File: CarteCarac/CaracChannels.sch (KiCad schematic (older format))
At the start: 6 parts

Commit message: Routé, verif pre-envoie
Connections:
- net +34 is gone; now on net +R34: SW_X32-34.3
- net -32 is gone; now on net +R34: SW_X32-34.12
- net -34 is gone; now on net -R34: SW_X32-34.11, SW_X32-34.6
- net -R32 is gone; now on net +R34: SW_X32-34.4
- net In2N is gone; now on net +R34: SW_X32-34.15, SW_X32-34.16
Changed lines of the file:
@@
 $Descr A4 11693 8268
 encoding utf-8
-Sheet 5 5
+Sheet 3 5
 Title "SCM Channels"
 Date "2019-10-22"
@@
 Comment4 "Route de Saclay \\nF-91128 Palaiseau \\nFrance"
 $EndDescr
-Text HLabel 3450 2450 2    50   Input ~ 0
+Text HLabel 3525 2450 2    50   Input ~ 0
 Pot_Offset2
-Text HLabel 3450 2050 2    50   Input ~ 0
+Text HLabel 3525 2050 2    50   Input ~ 0
 Pot_Offset1
 Connection ~ 2075 2050
@@
 	3250 2850 3375 2850
 Wire Wire Line
-	3450 2050 3250 2050
-Wire Wire Line
-	3450 2450 3250 2450
+	3525 2050 3250 2050
+Wire Wire Line
+	3525 2450 3250 2450
 Text Label 3375 2950 0    50   ~ 0
 +32
 Text Label 3375 3350 0    50   ~ 0
 -32
-Text Label 3300 2550 0    50   ~ 0
+Text Label 3375 2550 0    50   ~ 0
 -34
-Text Label 3300 2150 0    50   ~ 0
+Text Label 3400 2150 0    50   ~ 0
 +34
 Wire Wire Line
-	3250 2550 3300 2550
-Wire Wire Line
-	3250 2150 3300 2150
+	3250 2550 3375 2550
+Wire Wire Line
+	3250 2150 3400 2150
 Wire Wire Line
 	3250 3350 3375 3350
@@
 	3250 2950 3375 2950
 Wire Wire Line
-	3250 3150 3650 3150
-Wire Wire Line
-	3250 2750 3650 2750
-Wire Wire Line
-	3650 2350 3250 2350
-Wire Wire Line
-	3650 1950 3250 1950
+	3250 3150 4100 3150
+Wire Wire Line
+	3250 2750 4050 2750
+Wire Wire Line
+	4100 2350 4050 2350
+Wire Wire Line
+	4100 1950 3250 1950
 Wire Wire Line
 	2250 3250 2350 3250
@@
 AR Path="/5D6520CE/5D843251/5E294A95" Ref="RV_Z32-34"  Part="1"
 AR Path="/5D6520CE/5D83A418/5E294A95" Ref="RV_Y32-34"  Part="1"
-F 0 "RV_X32-34" V 1868 2250 50  0000 C CNN
+F 0 "RV_Y32-34" V 1868 2250 50  0000 C CNN
 F 1 "5K" V 1959 2250 50  0000 C CNN
 F 2 "LibPersoNadj:Potentiometer_Bourns_3683S" H 2075 2250 50  0001 C CNN
@@
 AR Path="/5D6520CE/5D843251/5E1E5B8A" Ref="SW_Z32-34"  Part="1"
 AR Path="/5D6520CE/5D83A418/5E1E5B8A" Ref="SW_Y32-34"  Part="1"
-F 0 "SW_X32-34" H 2800 1725 50  0000 C CNN
+F 0 "SW_Y32-34" H 2800 1725 50  0000 C CNN
 F 1 "SW_Rotary4x3" H 2800 1816 50  0000 C CNN
 F 2 "LibPersoNadj:Switch_4P3T_MRA403_NKK_Turned30°" H 2650 3550 50  0001 C CNN
@@
 AR Path="/5D6520CE/5D843251/5E1D214E" Ref="SW_RZ10"  Part="1"
 AR Path="/5D6520CE/5D83A418/5E1D214E" Ref="SW_RY10"  Part="1"
-F 0 "SW_RX10" H 3050 5060 50  0000 C CNN
+F 0 "SW_RY10" H 3050 5060 50  0000 C CNN
 F 1 "SW_Push_DPDT" H 3050 4969 50  0000 C CNN
 F 2 "LibPersoNadj:SW_NKK_DPDT_B22AP" H 3050 4775 50  0001 C CNN
@@
 AR Path="/5D6520CE/5D843251/5E28B2BF" Ref="RVZ10"  Part="1"
 AR Path="/5D6520CE/5D83A418/5E28B2BF" Ref="RVY10"  Part="1"
-F 0 "RVX10" V 2575 4675 50  0000 R CNN
+F 0 "RVY10" V 2575 4675 50  0000 R CNN
 F 1 "12K" V 2900 4650 50  0000 R CNN
 F 2 "LibPersoNadj:Potentiometer_Bourns_3683S" H 2675 4575 50  0001 C CNN
@@
 AR Path="/5D6520CE/5D843251/5E1CF71F" Ref="SW_RZ12"  Part="1"
 AR Path="/5D6520CE/5D83A418/5E1CF71F" Ref="SW_RY12"  Part="1"
-F 0 "SW_RX12" H 3075 6460 50  0000 C CNN
+F 0 "SW_RY12" H 3075 6460 50  0000 C CNN
 F 1 "SW_Push_DPDT" H 3075 6369 50  0000 C CNN
 F 2 "LibPersoNadj:SW_NKK_DPDT_B22AP" H 3075 6175 50  0001 C CNN
@@
 AR Path="/5D6520CE/5D843251/5E1C7841" Ref="RVZ12"  Part="1"
 AR Path="/5D6520CE/5D83A418/5E1C7841" Ref="RVY12"  Part="1"
-F 0 "RVX12" H 2655 5929 50  0000 R CNN
+F 0 "RVY12" H 2655 5929 50  0000 R CNN
 F 1 "16K" H 2655 6020 50  0000 R CNN
 F 2 "LibPersoNadj:Potentiometer_Bourns_3683S" H 2725 5975 50  0001 C CNN
@@
 Text HLabel 3400 6275 2    50   Input ~ 0
 -R12
-Text HLabel 3650 1950 2    50   Input ~ 0
+Text HLabel 4100 1950 2    50   Input ~ 0
 +R32
-Text HLabel 3650 2350 2    50   Input ~ 0
+Text HLabel 4100 2350 2    50   Input ~ 0
 -R32
-Text HLabel 3650 2750 2    50   Input ~ 0
+Text HLabel 4100 2750 2    50   Input ~ 0
 +R34
-Text HLabel 3650 3150 2    50   Input ~ 0
+Text HLabel 4100 3150 2    50   Input ~ 0
 -R34
+Text Label 4050 2575 0    50   ~ 0
+In2N
+Wire Wire Line
+	4050 2350 4050 2750
+Connection ~ 4050 2350
+Wire Wire Line
+	4050 2350 3250 2350
+Connection ~ 4050 2750
+Wire Wire Line
+	4050 2750 4100 2750
+Text Label 3375 3150 0    50   ~ 0
+-34
+Text Label 3400 2350 0    50   ~ 0
+-32
+Text Label 3375 2750 0    50   ~ 0
++34
 $EndSCHEMATC

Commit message: Envoyé en prod
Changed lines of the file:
@@
 $Descr A4 11693 8268
 encoding utf-8
-Sheet 3 5
+Sheet 5 5
 Title "SCM Channels"
 Date "2019-10-22"
@@
 AR Path="/5D6520CE/5D843251/5E294A95" Ref="RV_Z32-34"  Part="1"
 AR Path="/5D6520CE/5D83A418/5E294A95" Ref="RV_Y32-34"  Part="1"
-F 0 "RV_Y32-34" V 1868 2250 50  0000 C CNN
+F 0 "RV_X32-34" V 1868 2250 50  0000 C CNN
 F 1 "5K" V 1959 2250 50  0000 C CNN
 F 2 "LibPersoNadj:Potentiometer_Bourns_3683S" H 2075 2250 50  0001 C CNN
@@
 AR Path="/5D6520CE/5D843251/5E1E5B8A" Ref="SW_Z32-34"  Part="1"
 AR Path="/5D6520CE/5D83A418/5E1E5B8A" Ref="SW_Y32-34"  Part="1"
-F 0 "SW_Y32-34" H 2800 1725 50  0000 C CNN
+F 0 "SW_X32-34" H 2800 1725 50  0000 C CNN
 F 1 "SW_Rotary4x3" H 2800 1816 50  0000 C CNN
 F 2 "LibPersoNadj:Switch_4P3T_MRA403_NKK_Turned30°" H 2650 3550 50  0001 C CNN
@@
 AR Path="/5D6520CE/5D843251/5E1D214E" Ref="SW_RZ10"  Part="1"
 AR Path="/5D6520CE/5D83A418/5E1D214E" Ref="SW_RY10"  Part="1"
-F 0 "SW_RY10" H 3050 5060 50  0000 C CNN
+F 0 "SW_RX10" H 3050 5060 50  0000 C CNN
 F 1 "SW_Push_DPDT" H 3050 4969 50  0000 C CNN
 F 2 "LibPersoNadj:SW_NKK_DPDT_B22AP" H 3050 4775 50  0001 C CNN
@@
 AR Path="/5D6520CE/5D843251/5E28B2BF" Ref="RVZ10"  Part="1"
 AR Path="/5D6520CE/5D83A418/5E28B2BF" Ref="RVY10"  Part="1"
-F 0 "RVY10" V 2575 4675 50  0000 R CNN
+F 0 "RVX10" V 2575 4675 50  0000 R CNN
 F 1 "12K" V 2900 4650 50  0000 R CNN
 F 2 "LibPersoNadj:Potentiometer_Bourns_3683S" H 2675 4575 50  0001 C CNN
@@
 AR Path="/5D6520CE/5D843251/5E1CF71F" Ref="SW_RZ12"  Part="1"
 AR Path="/5D6520CE/5D83A418/5E1CF71F" Ref="SW_RY12"  Part="1"
-F 0 "SW_RY12" H 3075 6460 50  0000 C CNN
+F 0 "SW_RX12" H 3075 6460 50  0000 C CNN
 F 1 "SW_Push_DPDT" H 3075 6369 50  0000 C CNN
 F 2 "LibPersoNadj:SW_NKK_DPDT_B22AP" H 3075 6175 50  0001 C CNN
@@
 AR Path="/5D6520CE/5D843251/5E1C7841" Ref="RVZ12"  Part="1"
 AR Path="/5D6520CE/5D83A418/5E1C7841" Ref="RVY12"  Part="1"
-F 0 "RVY12" H 2655 5929 50  0000 R CNN
+F 0 "RVX12" H 2655 5929 50  0000 R CNN
 F 1 "16K" H 2655 6020 50  0000 R CNN
 F 2 "LibPersoNadj:Potentiometer_Bourns_3683S" H 2725 5975 50  0001 C CNN

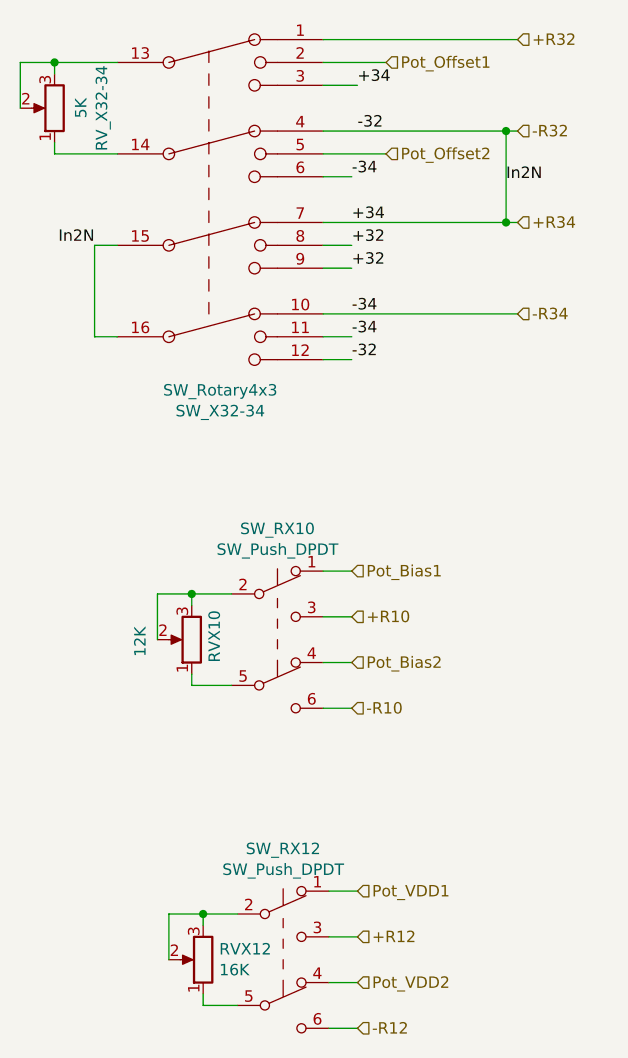
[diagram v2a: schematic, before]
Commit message: Correction pinout 6P3T & ajout d'étiquettes sur pin hiérarchique 3P4T + routage
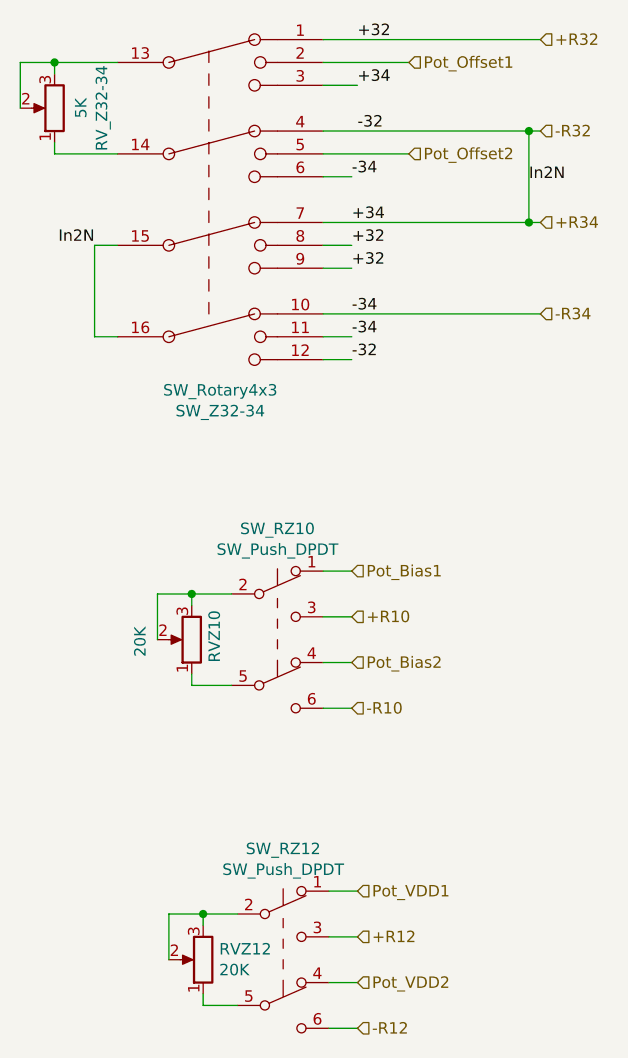
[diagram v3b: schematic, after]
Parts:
- RVX10: value 12K -> 20K
- RVX12: value 16K -> 20K
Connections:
- net +32 is gone; now on net +R32: SW_X32-34.8, SW_X32-34.9
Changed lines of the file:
@@
 $Descr A4 11693 8268
 encoding utf-8
-Sheet 5 5
+Sheet 4 5
 Title "SCM Channels"
 Date "2019-10-22"
@@
 Comment4 "Route de Saclay \\nF-91128 Palaiseau \\nFrance"
 $EndDescr
-Text HLabel 3525 2450 2    50   Input ~ 0
+Text HLabel 3625 2450 2    50   Input ~ 0
 Pot_Offset2
-Text HLabel 3525 2050 2    50   Input ~ 0
+Text HLabel 3625 2050 2    50   Input ~ 0
 Pot_Offset1
 Connection ~ 2075 2050
@@
 	3250 2850 3375 2850
 Wire Wire Line
-	3525 2050 3250 2050
-Wire Wire Line
-	3525 2450 3250 2450
+	3625 2050 3250 2050
+Wire Wire Line
+	3625 2450 3250 2450
 Text Label 3375 2950 0    50   ~ 0
 +32
@@
 	3250 2950 3375 2950
 Wire Wire Line
-	3250 3150 4100 3150
-Wire Wire Line
-	3250 2750 4050 2750
-Wire Wire Line
-	4100 2350 4050 2350
-Wire Wire Line
-	4100 1950 3250 1950
+	3250 3150 4200 3150
+Wire Wire Line
+	3250 2750 4150 2750
+Wire Wire Line
+	4200 2350 4150 2350
+Wire Wire Line
+	4200 1950 3250 1950
 Wire Wire Line
 	2250 3250 2350 3250
@@
 AR Path="/5D6520CE/5D843251/5E294A95" Ref="RV_Z32-34"  Part="1"
 AR Path="/5D6520CE/5D83A418/5E294A95" Ref="RV_Y32-34"  Part="1"
-F 0 "RV_X32-34" V 1868 2250 50  0000 C CNN
+F 0 "RV_Z32-34" V 1868 2250 50  0000 C CNN
 F 1 "5K" V 1959 2250 50  0000 C CNN
 F 2 "LibPersoNadj:Potentiometer_Bourns_3683S" H 2075 2250 50  0001 C CNN
@@
 AR Path="/5D6520CE/5D843251/5E1E5B8A" Ref="SW_Z32-34"  Part="1"
 AR Path="/5D6520CE/5D83A418/5E1E5B8A" Ref="SW_Y32-34"  Part="1"
-F 0 "SW_X32-34" H 2800 1725 50  0000 C CNN
+F 0 "SW_Z32-34" H 2800 1725 50  0000 C CNN
 F 1 "SW_Rotary4x3" H 2800 1816 50  0000 C CNN
 F 2 "LibPersoNadj:Switch_4P3T_MRA403_NKK_Turned30°" H 2650 3550 50  0001 C CNN
@@
 AR Path="/5D6520CE/5D843251/5E1D214E" Ref="SW_RZ10"  Part="1"
 AR Path="/5D6520CE/5D83A418/5E1D214E" Ref="SW_RY10"  Part="1"
-F 0 "SW_RX10" H 3050 5060 50  0000 C CNN
+F 0 "SW_RZ10" H 3050 5060 50  0000 C CNN
 F 1 "SW_Push_DPDT" H 3050 4969 50  0000 C CNN
 F 2 "LibPersoNadj:SW_NKK_DPDT_B22AP" H 3050 4775 50  0001 C CNN
@@
 AR Path="/5D6520CE/5D843251/5E28B2BF" Ref="RVZ10"  Part="1"
 AR Path="/5D6520CE/5D83A418/5E28B2BF" Ref="RVY10"  Part="1"
-F 0 "RVX10" V 2575 4675 50  0000 R CNN
-F 1 "12K" V 2900 4650 50  0000 R CNN
+F 0 "RVZ10" V 2575 4675 50  0000 R CNN
+F 1 "20K" V 2900 4650 50  0000 R CNN
 F 2 "LibPersoNadj:Potentiometer_Bourns_3683S" H 2675 4575 50  0001 C CNN
 F 3 "~" H 2675 4575 50  0001 C CNN
@@
 AR Path="/5D6520CE/5D843251/5E1CF71F" Ref="SW_RZ12"  Part="1"
 AR Path="/5D6520CE/5D83A418/5E1CF71F" Ref="SW_RY12"  Part="1"
-F 0 "SW_RX12" H 3075 6460 50  0000 C CNN
+F 0 "SW_RZ12" H 3075 6460 50  0000 C CNN
 F 1 "SW_Push_DPDT" H 3075 6369 50  0000 C CNN
 F 2 "LibPersoNadj:SW_NKK_DPDT_B22AP" H 3075 6175 50  0001 C CNN
@@
 AR Path="/5D6520CE/5D843251/5E1C7841" Ref="RVZ12"  Part="1"
 AR Path="/5D6520CE/5D83A418/5E1C7841" Ref="RVY12"  Part="1"
-F 0 "RVX12" H 2655 5929 50  0000 R CNN
-F 1 "16K" H 2655 6020 50  0000 R CNN
+F 0 "RVZ12" H 2655 5929 50  0000 R CNN
+F 1 "20K" H 2655 6020 50  0000 R CNN
 F 2 "LibPersoNadj:Potentiometer_Bourns_3683S" H 2725 5975 50  0001 C CNN
 F 3 "~" H 2725 5975 50  0001 C CNN
@@
 Text HLabel 3400 6275 2    50   Input ~ 0
 -R12
-Text HLabel 4100 1950 2    50   Input ~ 0
+Text HLabel 4200 1950 2    50   Input ~ 0
 +R32
-Text HLabel 4100 2350 2    50   Input ~ 0
+Text HLabel 4200 2350 2    50   Input ~ 0
 -R32
-Text HLabel 4100 2750 2    50   Input ~ 0
+Text HLabel 4200 2750 2    50   Input ~ 0
 +R34
-Text HLabel 4100 3150 2    50   Input ~ 0
+Text HLabel 4200 3150 2    50   Input ~ 0
 -R34
-Text Label 4050 2575 0    50   ~ 0
+Text Label 4150 2575 0    50   ~ 0
 In2N
 Wire Wire Line
-	4050 2350 4050 2750
-Connection ~ 4050 2350
-Wire Wire Line
-	4050 2350 3250 2350
-Connection ~ 4050 2750
-Wire Wire Line
-	4050 2750 4100 2750
+	4150 2350 4150 2750
+Connection ~ 4150 2350
+Wire Wire Line
+	4150 2350 3250 2350
+Connection ~ 4150 2750
+Wire Wire Line
+	4150 2750 4200 2750
 Text Label 3375 3150 0    50   ~ 0
 -34
@@
 Text Label 3375 2750 0    50   ~ 0
 +34
+Text Label 3400 1950 0    50   ~ 0
++32
 $EndSCHEMATC
